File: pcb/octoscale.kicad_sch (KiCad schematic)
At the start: 104 parts, among them J1 USB_C_Receptacle_USB2.0 TYPE-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, J2 Conn_01x04_Male, J3 Molex picoblade vertical C122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, J4 JST-SH, stemma, J5 JST-SH, J6 JST-SH, J7 Conn_01x04_Male, Q1 AO3415_C181094, Q2 MMBT44032T, Q3 S8050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

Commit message: Move Batt sense to adc capable pin
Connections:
- net BATT_SENSE: now also U5.10 (GPIO17/U1TXD/ADC2_CH6); no longer U5.23 (GPIO21)
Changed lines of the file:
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@@
     )
   )
-  (global_label "BATT_SENSE" (shape input) (at 177.8 173.99 0) (fields_autoplaced)
-    (effects (font (size 1.27 1.27)) (justify left))
-    (property "Intersheet References" "${INTERSHEET_REFS}" (id 0) (at 191.5221 174.0694 0)
-      (effects (font (size 1.27 1.27)) (justify left) hide)
+  (global_label "BATT_SENSE" (shape input) (at 59.69 205.74 180) (fields_autoplaced)
+    (effects (font (size 1.27 1.27)) (justify right))
+    (property "Intersheet References" "${INTERSHEET_REFS}" (id 0) (at 45.9679 205.6606 0)
+      (effects (font (size 1.27 1.27)) (justify right) hide)
     )
   )

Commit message: Change zener footprint
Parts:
- D16: footprint Diode_SMD:D_SOD-523 -> Diode_SMD:D_SOD-323
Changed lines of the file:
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@@
       (effects (font (size 1.27 1.27)) (justify left))
     )
-    (property "Footprint" "Diode_SMD:D_SOD-523" (id 2) (at 148.336 46.101 90)
+    (property "Footprint" "Diode_SMD:D_SOD-323" (id 2) (at 148.336 46.101 90)
       (effects (font (size 1.27 1.27)) hide)
     )
@@
     )
     (path "/d8709094-c0a5-4903-a813-2e8a6969aa9b"
-      (reference "D16") (unit 1) (value "3v Zener, BZT52C3V0T") (footprint "Diode_SMD:D_SOD-523")
+      (reference "D16") (unit 1) (value "3v Zener, BZT52C3V0T") (footprint "Diode_SMD:D_SOD-323")
     )
     (path "/84ee92d0-8911-4b51-a476-6cdc8fcc07e4"

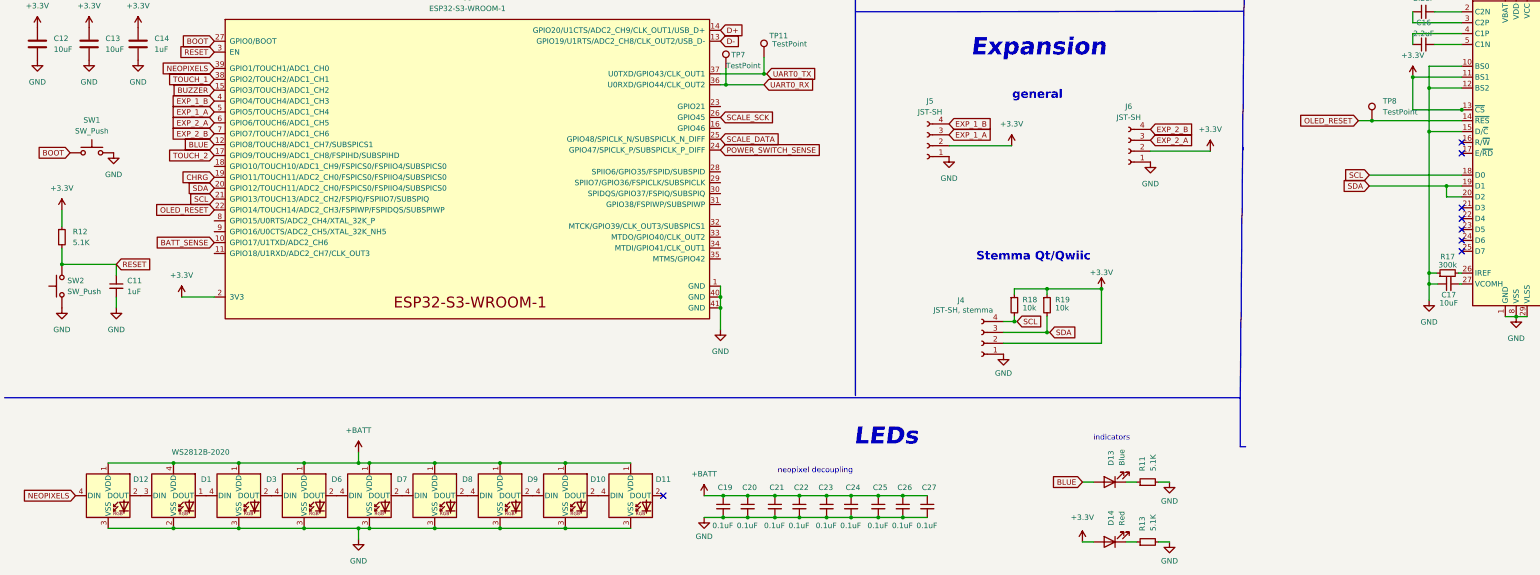
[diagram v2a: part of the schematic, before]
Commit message: Fix neopixel footprint
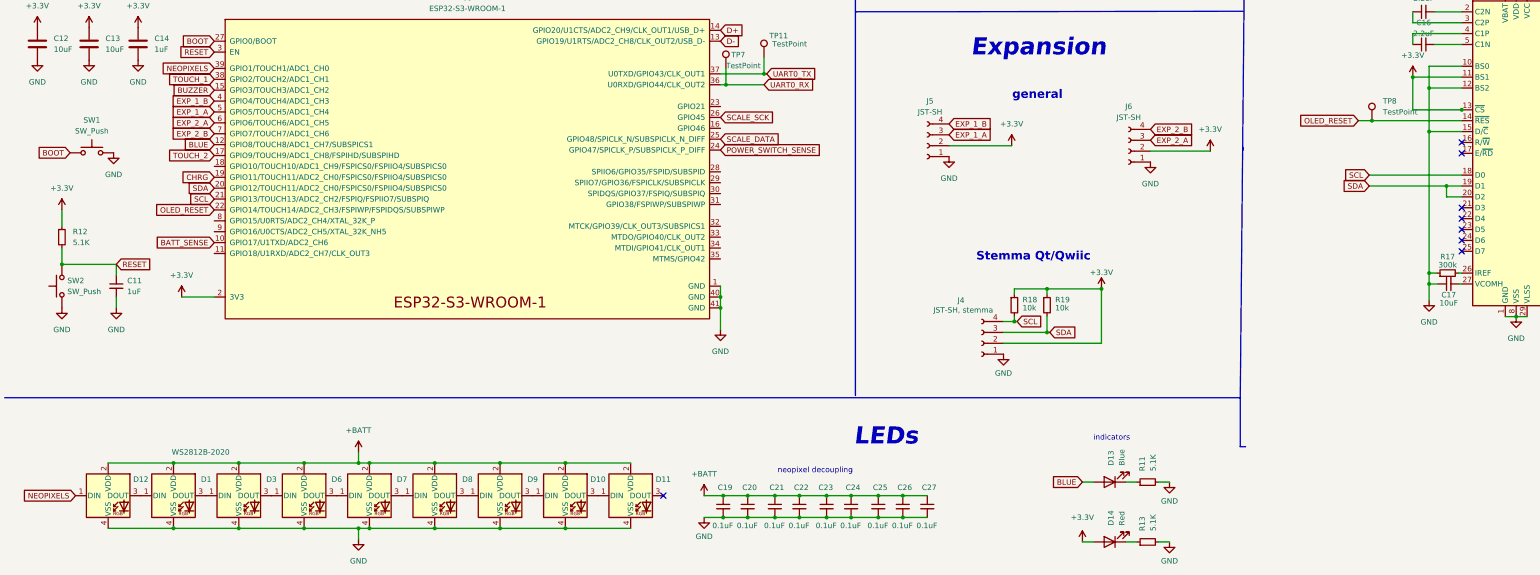
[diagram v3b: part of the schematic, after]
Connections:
- net +BATT: now also D1.2 (VDD), D10.2 (VDD), D11.2 (VDD), D12.2 (VDD), D3.2 (VDD), D6.2 (VDD), D7.2 (VDD), D8.2 (VDD), D9.2 (VDD); no longer D1.4 (VDD), D10.1 (VDD), D11.1 (VDD), D12.1 (VDD), D3.1 (VDD), D6.1 (VDD), D7.1 (VDD), D8.1 (VDD), D9.1 (VDD)
- net GND: now also D1.4 (VSS), D10.4 (VSS), D11.4 (VSS), D12.4 (VSS), D3.4 (VSS), D6.4 (VSS), D7.4 (VSS), D8.4 (VSS), D9.4 (VSS); no longer D1.2 (VSS), D10.3 (VSS), D11.3 (VSS), D12.3 (VSS), D3.3 (VSS), D6.3 (VSS), D7.3 (VSS), D8.3 (VSS), D9.3 (VSS)
- net NEOPIXELS: now also D12.1 (DIN); no longer D12.4 (DIN)
- net at D1.3 (DOUT): now also D3.1 (DIN); no longer D12.2 (DOUT)
- net at D1.1 (DIN): now also D12.3 (DOUT); no longer D3.4 (DIN)
- new net: D7.3 (DOUT), D8.1 (DIN)
- new net: D8.3 (DOUT), D9.1 (DIN)
- new net: D10.1 (DIN), D9.3 (DOUT)
- new net: D10.3 (DOUT), D11.1 (DIN)
- new net: D3.3 (DOUT), D6.1 (DIN)
- new net: D6.3 (DOUT), D7.1 (DIN)
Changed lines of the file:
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@@
   (junction (at 184.15 264.795) (diameter 0) (color 0 0 0 0)
   )
+  (junction (at 350.774 174.752) (diameter 0) (color 0 0 0 0)
+  )
   (junction (at 15.875 83.82) (diameter 0) (color 0 0 0 0)
   )
@@
   (junction (at 177.8 220.98) (diameter 0) (color 0 0 0 0)
   )
-  (junction (at 350.774 174.752) (diameter 0) (color 0 0 0 0)
-  )
   (junction (at 187.96 166.37) (diameter 0) (color 0 0 0 0)
   )
@@
     (stroke (width 0) (type default) (color 0 0 0 0))
   )
-  (wire (pts (xy 350.774 174.752) (xy 339.344 174.752))
-    (stroke (width 0) (type default) (color 0 0 0 0))
-  )
   (wire (pts (xy 95.885 272.415) (xy 111.125 272.415))
     (stroke (width 0) (type default) (color 0 0 0 0))
@@
     (stroke (width 0) (type default) (color 0 0 0 0))
   )
-  (wire (pts (xy 339.344 174.752) (xy 339.344 167.132))
-    (stroke (width 0) (type default) (color 0 0 0 0))
-  )
   (wire (pts (xy 259.08 89.154) (xy 257.81 89.154))
     (stroke (width 0) (type default) (color 0 0 0 0))
@@
     (stroke (width 0) (type default) (color 0 0 0 0))
   )
+  (wire (pts (xy 350.774 174.752) (xy 351.028 174.752))
+    (stroke (width 0) (type default) (color 0 0 0 0))
+  )
   (wire (pts (xy 105.918 77.216) (xy 97.028 77.216))
     (stroke (width 0) (type default) (color 0 0 0 0))
@@
     (stroke (width 0) (type default) (color 0 0 0 0))
   )
+  (wire (pts (xy 339.344 174.752) (xy 350.774 174.752))
+    (stroke (width 0) (type default) (color 0 0 0 0))
+  )
   (wire (pts (xy 375.158 141.732) (xy 375.158 143.002))
     (stroke (width 0) (type default) (color 0 0 0 0))
@@
     (stroke (width 0) (type default) (color 0 0 0 0))
   )
-  (wire (pts (xy 351.028 174.752) (xy 350.774 174.752))
+  (wire (pts (xy 339.344 167.132) (xy 339.344 174.752))
     (stroke (width 0) (type default) (color 0 0 0 0))
   )
@@
     (pin "1")
   )
-  (symbol (lib_id "LED:WS2812B") (at 111.125 264.795 0) (unit 1)
+  (symbol (lib_name "WS2812B_6") (lib_id "LED:WS2812B") (at 111.125 264.795 0) (unit 1)
     (in_bom yes) (on_board yes)
     (property "Reference" "D8" (id 0) (at 118.745 260.985 0))
@@
     (pin "9")
   )
-  (symbol (lib_id "LED:WS2812B") (at 34.925 264.795 0) (unit 1)
+  (symbol (lib_name "WS2812B_2") (lib_id "LED:WS2812B") (at 34.925 264.795 0) (unit 1)
     (in_bom yes) (on_board yes)
     (property "Reference" "D12" (id 0) (at 42.545 260.985 0))
@@
     (pin "2")
   )
-  (symbol (lib_id "LED:WS2812B") (at 141.605 264.795 0) (unit 1)
+  (symbol (lib_name "WS2812B_8") (lib_id "LED:WS2812B") (at 141.605 264.795 0) (unit 1)
     (in_bom yes) (on_board yes)
     (property "Reference" "D10" (id 0) (at 149.225 260.985 0))
@@
     (pin "4")
   )
-  (symbol (lib_id "LED:WS2812B") (at 126.365 264.795 0) (unit 1)
+  (symbol (lib_name "WS2812B_7") (lib_id "LED:WS2812B") (at 126.365 264.795 0) (unit 1)
     (in_bom yes) (on_board yes)
     (property "Reference" "D9" (id 0) (at 133.985 260.985 0))
@@
       (effects (font (size 1.27 1.27)) (justify left top) hide)
     )
-    (pin "1")
     (pin "2")
     (pin "3")
     (pin "4")
+    (pin "1")
   )
   (symbol (lib_id "power:GND") (at 355.6 143.51 0) (unit 1)
@@
     (pin "3")
   )
-  (symbol (lib_id "LED:WS2812B") (at 80.645 264.795 0) (unit 1)
+  (symbol (lib_name "WS2812B_4") (lib_id "LED:WS2812B") (at 80.645 264.795 0) (unit 1)
     (in_bom yes) (on_board yes)
     (property "Reference" "D6" (id 0) (at 88.265 260.985 0))
@@
     (pin "2")
   )
-  (symbol (lib_id "LED:WS2812B") (at 65.405 264.795 0) (unit 1)
+  (symbol (lib_name "WS2812B_3") (lib_id "LED:WS2812B") (at 65.405 264.795 0) (unit 1)
     (in_bom yes) (on_board yes)
     (property "Reference" "D3" (id 0) (at 73.025 260.985 0))
@@
     (pin "2")
   )
-  (symbol (lib_id "LED:WS2812B") (at 95.885 264.795 0) (unit 1)
+  (symbol (lib_name "WS2812B_5") (lib_id "LED:WS2812B") (at 95.885 264.795 0) (unit 1)
     (in_bom yes) (on_board yes)
     (property "Reference" "D7" (id 0) (at 103.505 260.985 0))
@@
       (effects (font (size 1.27 1.27)) (justify left top) hide)
     )
-    (pin "1")
-    (pin "2")
     (pin "3")
     (pin "4")
+    (pin "1")
+    (pin "2")
   )
   (symbol (lib_id "power:VBUS") (at 97.028 72.136 0) (unit 1)

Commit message: Slight tweaks
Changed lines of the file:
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@@
   (junction (at 184.15 264.795) (diameter 0) (color 0 0 0 0)
   )
-  (junction (at 350.774 174.752) (diameter 0) (color 0 0 0 0)
-  )
   (junction (at 15.875 83.82) (diameter 0) (color 0 0 0 0)
   )
@@
     (stroke (width 0) (type default) (color 0 0 0 0))
   )
+  (wire (pts (xy 339.344 167.132) (xy 339.344 174.752))
+    (stroke (width 0) (type default) (color 0 0 0 0))
+  )
   (wire (pts (xy 65.405 272.415) (xy 80.645 272.415))
     (stroke (width 0) (type default) (color 0 0 0 0))
@@
     (stroke (width 0) (type default) (color 0 0 0 0))
   )
-  (wire (pts (xy 350.774 174.752) (xy 351.028 174.752))
+  (wire (pts (xy 339.344 174.752) (xy 350.774 174.752))
     (stroke (width 0) (type default) (color 0 0 0 0))
   )
@@
     (stroke (width 0) (type default) (color 0 0 0 0))
   )
+  (wire (pts (xy 339.344 166.624) (xy 339.344 167.132))
+    (stroke (width 0) (type default) (color 0 0 0 0))
+  )
   (polyline (pts (xy 325.755 109.855) (xy 325.755 12.065))
     (stroke (width 0) (type default) (color 0 0 0 0))
@@
     (stroke (width 0) (type default) (color 0 0 0 0))
   )
-  (wire (pts (xy 339.344 174.752) (xy 350.774 174.752))
-    (stroke (width 0) (type default) (color 0 0 0 0))
-  )
   (wire (pts (xy 375.158 141.732) (xy 375.158 143.002))
     (stroke (width 0) (type default) (color 0 0 0 0))
@@
     (stroke (width 0) (type default) (color 0 0 0 0))
   )
-  (wire (pts (xy 339.344 167.132) (xy 339.344 174.752))
-    (stroke (width 0) (type default) (color 0 0 0 0))
-  )
   (wire (pts (xy 246.38 94.234) (xy 257.81 94.234))
     (stroke (width 0) (type default) (color 0 0 0 0))
@@
   (symbol (lib_id "Device:C_Small") (at 341.884 159.512 90) (unit 1)
     (in_bom yes) (on_board yes)
-    (property "Reference" "C16" (id 0) (at 341.884 154.432 90))
+    (property "Reference" "C16" (id 0) (at 341.884 155.194 90))
     (property "Value" "2.2uF" (id 1) (at 341.884 156.972 90))
     (property "Footprint" "Capacitor_SMD:C_0805_2012Metric_Pad1.18x1.45mm_HandSolder" (id 2) (at 341.884 159.512 0)
@@
     (pin "2")
   )
-  (symbol (lib_id "power:+3.3V") (at 339.344 167.132 0) (unit 1)
-    (in_bom yes) (on_board yes) (fields_autoplaced)
-    (property "Reference" "#PWR046" (id 0) (at 339.344 170.942 0)
+  (symbol (lib_id "power:+3.3V") (at 339.344 166.624 0) (unit 1)
+    (in_bom yes) (on_board yes)
+    (property "Reference" "#PWR046" (id 0) (at 339.344 170.434 0)
       (effects (font (size 1.27 1.27)) hide)
     )
-    (property "Value" "+3.3V" (id 1) (at 339.344 162.052 0))
-    (property "Footprint" "" (id 2) (at 339.344 167.132 0)
+    (property "Value" "+3.3V" (id 1) (at 339.344 163.068 0))
+    (property "Footprint" "" (id 2) (at 339.344 166.624 0)
       (effects (font (size 1.27 1.27)) hide)
     )
-    (property "Datasheet" "" (id 3) (at 339.344 167.132 0)
+    (property "Datasheet" "" (id 3) (at 339.344 166.624 0)
       (effects (font (size 1.27 1.27)) hide)
     )
@@
   )
   (symbol (lib_id "Device:R_Small") (at 277.495 275.59 90) (unit 1)
-    (in_bom yes) (on_board yes) (fields_autoplaced)
-    (property "Reference" "R13" (id 0) (at 276.2249 273.05 0)
+    (in_bom yes) (on_board yes)
+    (property "Reference" "R13" (id 0) (at 279.4 270.764 90)
       (effects (font (size 1.27 1.27)) (justify left))
     )
-    (property "Value" "5.1K" (id 1) (at 278.7649 273.05 0)
+    (property "Value" "5.1K" (id 1) (at 279.4 273.304 90)
       (effects (font (size 1.27 1.27)) (justify left))
     )
@@
   )
   (symbol (lib_id "Device:R_Small") (at 277.495 261.62 90) (unit 1)
-    (in_bom yes) (on_board yes) (fields_autoplaced)
-    (property "Reference" "R11" (id 0) (at 276.2249 259.08 0)
+    (in_bom yes) (on_board yes)
+    (property "Reference" "R11" (id 0) (at 279.4 256.794 90)
       (effects (font (size 1.27 1.27)) (justify left))
     )
-    (property "Value" "5.1K" (id 1) (at 278.7649 259.08 0)
+    (property "Value" "5.1K" (id 1) (at 279.4 259.334 90)
       (effects (font (size 1.27 1.27)) (justify left))
     )
@@
   )
   (symbol (lib_id "Device:LED") (at 268.605 261.62 180) (unit 1)
-    (in_bom yes) (on_board yes) (fields_autoplaced)
-    (property "Reference" "D13" (id 0) (at 268.9224 257.81 90)
+    (in_bom yes) (on_board yes)
+    (property "Reference" "D13" (id 0) (at 266.7 256.54 0)
       (effects (font (size 1.27 1.27)) (justify right))
     )
-    (property "Value" "Blue" (id 1) (at 271.4624 257.81 90)
+    (property "Value" "Blue" (id 1) (at 266.7 258.318 0)
       (effects (font (size 1.27 1.27)) (justify right))
     )
@@
   )
   (symbol (lib_id "Device:LED") (at 268.605 275.59 180) (unit 1)
-    (in_bom yes) (on_board yes) (fields_autoplaced)
-    (property "Reference" "D14" (id 0) (at 268.9224 271.78 90)
+    (in_bom yes) (on_board yes)
+    (property "Reference" "D14" (id 0) (at 266.954 270.002 0)
       (effects (font (size 1.27 1.27)) (justify right))
     )
-    (property "Value" "Red" (id 1) (at 271.4624 271.78 90)
+    (property "Value" "Red" (id 1) (at 266.954 272.034 0)
       (effects (font (size 1.27 1.27)) (justify right))
     )
